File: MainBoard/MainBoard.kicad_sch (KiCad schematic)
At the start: 96 parts, among them J1 KH-TYPE-C-16P, Q1 PMV19XNEAR, Q2 PMV19XNEAR, Q3 PMV19XNEAR, Q4 PMV19XNEAR, U1 INA185A4IDRLR, U10 SI3477DV-T1-GE3, U11 INA185A4IDRLR, U12 SI3477DV-T1-GE3, U2 SI3477DV-T1-GE3, U3 STM32L496VGY6PTR, U4 FUSB302BMPX, U5 BNO086, U6 TPS63802DLAR, U7 SI3477DV-T1-GE3, U8 BQ25756ERRVR, U9 TCAN332DCNR, Y1 9HT11-32.768KBZF-T

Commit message: imu changed from crystal to external mcu clock- yoshita
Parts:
- removed C24, C25: 22pF, Capacitor_SMD:C_0402_1005Metric, symbol Device:C
- removed Y1: 9HT11-32.768KBZF-T, Crystal:Crystal_SMD_2012-2Pin_2.0x1.2mm_HandSoldering, symbol Device:Crystal
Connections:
- net +3.3V: now also U5.10 (CLKSEL0), U5.26 (XOUT32/CLKSEL1)
- net IMU_MCO: now reaches U3.E1 (PC8)
- net IMU_MCO: now also U5.27 (XIN32)
- no-connect marks 23 -> 22

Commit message: Fixed values/issues on BQ chip
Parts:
- R19: value 25k -> 50k
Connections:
- net BAT_SIDE_INDUC: now also C42.1; no longer C42.2, U8.20 (BTST2)
- net EXTERNAL_SIDE_INDUC: no longer U8.26 (BTST1)
- net GND: no longer C41.2, C42.1
- new net: C42.2, U8.20 (BTST2)
- new net: C41.2, U8.26 (BTST1)
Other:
- moved on the sheet: C41, C42
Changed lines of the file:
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@@
 	)
 	(junction
-		(at 480.06 187.96)
-		(diameter 0)
-		(color 0 0 0 0)
-	)
-	(junction
 		(at 234.95 187.96)
 		(diameter 0)
@@
 	)
 	(junction
-		(at 478.79 185.42)
-		(diameter 0)
-		(color 0 0 0 0)
-	)
-	(junction
 		(at 354.33 205.74)
 		(diameter 0)
@@
 	(wire
 		(pts
-			(xy 480.06 187.96) (xy 483.87 187.96)
-		)
-		(stroke
-			(width 0)
-			(type default)
-		)
-	)
-	(wire
-		(pts
 			(xy 383.54 306.07) (xy 414.02 306.07)
 		)
@@
 	(wire
 		(pts
-			(xy 478.79 185.42) (xy 483.87 185.42)
-		)
-		(stroke
-			(width 0)
-			(type default)
-		)
-	)
-	(wire
-		(pts
 			(xy 214.63 203.2) (xy 220.98 203.2)
 		)
@@
 	(wire
 		(pts
+			(xy 476.25 185.42) (xy 483.87 185.42)
+		)
+		(stroke
+			(width 0)
+			(type default)
+		)
+	)
+	(wire
+		(pts
 			(xy 427.99 266.7) (xy 434.34 266.7)
 		)
@@
 	(wire
 		(pts
-			(xy 427.99 187.96) (xy 480.06 187.96)
+			(xy 427.99 187.96) (xy 476.25 187.96)
 		)
 		(stroke
@@
 	(wire
 		(pts
-			(xy 427.99 185.42) (xy 478.79 185.42)
+			(xy 427.99 185.42) (xy 468.63 185.42)
 		)
 		(stroke
@@
 	(wire
 		(pts
+			(xy 483.87 187.96) (xy 500.38 187.96)
+		)
+		(stroke
+			(width 0)
+			(type default)
+		)
+	)
+	(wire
+		(pts
 			(xy 351.79 212.09) (xy 344.17 212.09)
 		)
@@
 	(wire
 		(pts
-			(xy 478.79 182.88) (xy 478.79 185.42)
-		)
-		(stroke
-			(width 0)
-			(type default)
-		)
-	)
-	(wire
-		(pts
 			(xy 220.98 322.58) (xy 223.52 322.58)
 		)
@@
 	(global_label "BAT_SIDE_INDUC"
 		(shape input)
-		(at 483.87 187.96 0)
+		(at 500.38 187.96 0)
 		(fields_autoplaced yes)
 		(effects
@@
 		)
 		(property "Intersheetrefs" "${INTERSHEET_REFS}"
-			(at 502.1557 187.96 0)
+			(at 518.6657 187.96 0)
 			(effects
 				(font
@@
 	)
 	(symbol
-		(lib_id "power:GND")
-		(at 480.06 195.58 0)
-		(unit 1)
-		(exclude_from_sim no)
-		(in_bom yes)
-		(on_board yes)
-		(dnp no)
-		(fields_autoplaced yes)
-		(property "Reference" "#PWR064"
-			(at 480.06 201.93 0)
-			(effects
-				(font
-					(size 1.27 1.27)
-				)
-				(hide yes)
-			)
-		)
-		(property "Value" "GND"
-			(at 480.06 200.66 0)
-			(effects
-				(font
-					(size 1.27 1.27)
-				)
-			)
-		)
-		(property "Footprint" ""
-			(at 480.06 195.58 0)
-			(effects
-				(font
-					(size 1.27 1.27)
-				)
-				(hide yes)
-			)
-		)
-		(property "Datasheet" ""
-			(at 480.06 195.58 0)
-			(effects
-				(font
-					(size 1.27 1.27)
-				)
-				(hide yes)
-			)
-		)
-		(property "Description" "Power symbol creates a global label with name \"GND\" , ground"
-			(at 480.06 195.58 0)
-			(effects
-				(font
-					(size 1.27 1.27)
-				)
-				(hide yes)
-			)
-		)
-		(pin "1"
-		)
-		(instances
-			(project "MainBoard"
-				(path "/6b5bd430-8554-421d-a2d3-13f7e8cab430"
-					(reference "#PWR064")
-					(unit 1)
-				)
-			)
-		)
-	)
-	(symbol
 		(lib_id "Device:C")
 		(at 171.45 383.54 0)
@@
 			)
 		)
-		(property "Value" "25k"
+		(property "Value" "50k"
 			(at 362.204 213.868 90)
 			(effects
@@
 	(symbol
 		(lib_id "Device:C")
-		(at 478.79 179.07 180)
+		(at 472.44 185.42 270)
 		(unit 1)
 		(exclude_from_sim no)
@@
 		(dnp no)
 		(property "Reference" "C41"
-			(at 484.632 180.086 0)
+			(at 472.186 179.832 90)
 			(effects
 				(font
@@
 		)
 		(property "Value" "100nF"
-			(at 484.632 177.546 0)
+			(at 472.948 181.864 90)
 			(effects
 				(font
@@
 		)
 		(property "Footprint" "Capacitor_SMD:C_0402_1005Metric"
-			(at 477.8248 175.26 0)
+			(at 468.63 186.3852 0)
 			(effects
 				(font
@@
 		)
 		(property "Datasheet" "~"
-			(at 478.79 179.07 0)
+			(at 472.44 185.42 0)
 			(effects
 				(font
@@
 		)
 		(property "Description" "Unpolarized capacitor"
-			(at 478.79 179.07 0)
+			(at 472.44 185.42 0)
 			(effects
 				(font
@@
 	)
 	(symbol
-		(lib_id "power:GND")
-		(at 478.79 175.26 180)
-		(unit 1)
-		(exclude_from_sim no)
-		(in_bom yes)
-		(on_board yes)
-		(dnp no)
-		(fields_autoplaced yes)
-		(property "Reference" "#PWR063"
-			(at 478.79 168.91 0)
-			(effects
-				(font
-					(size 1.27 1.27)
-				)
-				(hide yes)
-			)
-		)
-		(property "Value" "GND"
-			(at 478.79 170.18 0)
-			(effects
-				(font
-					(size 1.27 1.27)
-				)
-			)
-		)
-		(property "Footprint" ""
-			(at 478.79 175.26 0)
-			(effects
-				(font
-					(size 1.27 1.27)
-				)
-				(hide yes)
-			)
-		)
-		(property "Datasheet" ""
-			(at 478.79 175.26 0)
-			(effects
-				(font
-					(size 1.27 1.27)
-				)
-				(hide yes)
-			)
-		)
-		(property "Description" "Power symbol creates a global label with name \"GND\" , ground"
-			(at 478.79 175.26 0)
-			(effects
-				(font
-					(size 1.27 1.27)
-				)
-				(hide yes)
-			)
-		)
-		(pin "1"
-		)
-		(instances
-			(project "MainBoard"
-				(path "/6b5bd430-8554-421d-a2d3-13f7e8cab430"
-					(reference "#PWR063")
-					(unit 1)
-				)
-			)
-		)
-	)
-	(symbol
 		(lib_id "inspirefly:INA185A1IDRLR")
 		(at 346.71 114.3 0)
@@
 	(symbol
 		(lib_id "Device:C")
-		(at 480.06 191.77 180)
+		(at 480.06 187.96 270)
 		(unit 1)
 		(exclude_from_sim no)
@@
 		(dnp no)
 		(property "Reference" "C42"
-			(at 485.648 193.04 0)
+			(at 484.378 189.484 90)
 			(effects
 				(font
@@
 		)
 		(property "Value" "100nF"
-			(at 485.648 190.5 0)
+			(at 484.378 192.024 90)
 			(effects
 				(font
@@
 		)
 		(property "Footprint" "Capacitor_SMD:C_0402_1005Metric"
-			(at 479.0948 187.96 0)
+			(at 476.25 188.9252 0)
 			(effects
 				(font
@@
 		)
 		(property "Datasheet" "~"
-			(at 480.06 191.77 0)
+			(at 480.06 187.96 0)
 			(effects
 				(font
@@
 		)
 		(property "Description" "Unpolarized capacitor"
-			(at 480.06 191.77 0)
+			(at 480.06 187.96 0)
 			(effects
 				(font

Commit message: Footprint edits and board setup
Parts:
- added TP1: BatBeforeCutoff, TestPoint:TestPoint_Pad_D1.0mm, symbol Connector:TestPoint
- added TP2: Bat+, TestPoint:TestPoint_Pad_D1.0mm, symbol Connector:TestPoint
- added TP3: 3.3V, TestPoint:TestPoint_Pad_D1.0mm, symbol Connector:TestPoint
- added TP4, TP5, TP6: GND, TestPoint:TestPoint_Pad_D1.0mm, symbol Connector:TestPoint
- JP1: footprint Jumper:SolderJumper-2_P1.3mm_Open_TrianglePad1.0x1.5mm -> inspirefly:SmallJumper
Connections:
- net +3.3V: now also TP3.1
- net BAT+: now also TP2.1
- net GND: now also TP4.1, TP5.1, TP6.1
- net at BT1.P, BT2.P, R13.2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: now also TP1.1

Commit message: Added a good amount of STM connections
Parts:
- removed R22: 250k, Resistor_SMD:R_0402_1005Metric, symbol Device:R_US
- added C24, C25: 100nF, Capacitor_SMD:C_0402_1005Metric, symbol Device:C_Small
- added R1, R2: 1k, Resistor_SMD:R_0402_1005Metric, symbol Device:R_US
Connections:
- net H_MDSI_MCUMOSI is gone; now on net H_MDSI_SPI1_MOSI: U5.17 (SA0/H_MOSI)
- net IMU_CSN_GPIO is gone; now on net IMU_SP1_NSS: U5.18 (H_CSN)
- net IMU_MCU_MISO is gone; now on net IMU_MCU_SPI1_MISO: U5.20 (H_SDA/H_MISO/TX)
- net IMU_MCU_SLK is gone; now on net IMU_MCU_SPI1_SCK: U5.19 (H_SCL/SCK/RX)
- net +3.3V: no longer U5.26 (XOUT32/CLKSEL1)
- net ADC1_A1: now also R1.1
- net ADC1_A2: now also R2.1
- net CAN_RXD: now also U3.B3 (PD0)
- net CAN_TXD: now also U3.A3 (PD1)
- net GND: now also U5.26 (XOUT32/CLKSEL1), U8.10 (ILIM_HIZ), C24.1, C25.2
- net I2C1_SCL: now also U3.B8 (PB8)
- net I2C1_SDA: now also U3.A8 (PB9)
- net I2C2_SCL: now also U3.H2 (PB13)
- net I2C2_SDA: now also U3.H1 (PB14)
- net I2C3_SCL: now also U3.G10 (PC0)
- net I2C3_SDA: now also U3.F7 (PC1)
- net I2C4_SCL: now also U3.A7 (PB6)
- net I2C4_SDA: now also U3.B7 (PB7)
- net IMU_PS0/WAKE_GPIO: no longer U3.G8 (PA0)
- net USB_D+: now also U3.C1 (PA12)
- net USB_D-: now also U3.D1 (PA11)
- net PARENT_SPI3_MISO: now reaches U3.A5 (PG10)
- net PARENT_SPI3_NSS: now reaches U3.B6 (PG12)
- net PARENT_SPI3_SCK: now reaches U3.D6 (PG9)
- net PARENT_SPI3_MOSI: now reaches U3.E5 (PG11)
- net ANT_SPI2_MOSI: now reaches U3.F6 (PC3)
- net H_MDSI_SPI1_MOSI: now reaches U3.G6 (PA7)
- net at U3.G7 (PA1): now also C24.2, R1.2
- net ANT_SPI2_MISO: now reaches U3.G9 (PC2)
- net IMU_SP1_NSS: now reaches U3.H7 (PA4)
- net at U3.H8 (PA2): now also C25.1, R2.2
- net ANT_SPI2_NSS: now reaches U3.J1 (PB12)
- net IMU_MCU_SPI1_SCK: now reaches U3.J7 (PA5)
- net ANT_SPI2_SCK: now reaches U3.K3 (PB10)
- net IMU_MCU_SPI1_MISO: now reaches U3.K9 (PA6)
- net IMU_NRST: now reaches U5.11 (NRST)
- net BQ_INT_DIN renamed BATMANG_INT_DIN
- net IMU_MCO: no longer names the net of U3.E1 (PC8)
- net IMU_MCO: no longer U5.27 (XIN32)
- net INT_N renamed USBC_PD_INT_N
- no-connect marks 22 -> 23
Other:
- moved on the sheet: U3A

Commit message: Pushing more schematic changes
Added ST link connections
Added Harwin M55
Changed some items for Battery managment
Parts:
- removed J1: KH-TYPE-C-16P, inspirefly:KINGHELM_KH-TYPE-C-16P, symbol inspirefly:KH-TYPE-C-16P
- added C29, C46: 22pF, Capacitor_SMD:C_0402_1005Metric, symbol Device:C_Small
- added J1: 0015912060 Molex, inspirefly:CONN_713080000-SD_06_M6p10_MOL, symbol Connector:Conn_01x06_Pin
- added J2: USB4110-GF-A, USB4110-GF-A_GCT, symbol inspirefly:USB4110-GF-A
- added J3: M55-7104042R, inspirefly:HARWIN_M55-7104042R, symbol inspirefly:M55-7104042R
- added R22: 100k, Resistor_SMD:R_0402_1005Metric, symbol Device:R_US
- added SW1, SW2: SW_TL1015AF160QG, inspirefly:SW_TL1015AF160QG, symbol Switch:SW_Push
- added Y1: XTAL_ABS07-32.768KHZ-T, inspirefly:XTAL_ABS07-32.768KHZ-T, symbol Device:Crystal
- L2: value 4.7uH -> 2.2uH; footprint inspirefly:WE-LQSA_5040 -> inspirefly:IHLP1212BZEZ2R2M1Z
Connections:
- net +3.3V: now also J1.5 (Pin_5), SW2.2
- net ANT_SPI2_MISO: now also J3.A15
- net ANT_SPI2_MOSI: now also J3.A16
- net ANT_SPI2_NSS: now also J3.A14
- net ANT_SPI2_SCK: now also J3.A13
- net BOARD_OUT_3.3V: now also J3.B1, J3.B2, J3.B3
- net BOARD_OUT_BAT: now also J3.B6, J3.B7, J3.B8
- net CAN_H: now also J3.A18
- net CAN_L: now also J3.A20
- net EXTERNAL_VOLTAGE: now also J3.B11, J3.B12, J3.B13, J3.B14
- net GND: now also C29.1, C46.1, J1.6 (Pin_6), J2.15 (Shield), J2.16 (Shield), J2.17 (Shield), J2.18 (Shield), J2.A1-B12 (GND), J2.A12-B1 (GND), J3.A17, J3.A19, J3.B10, J3.B18, J3.B20, J3.B4, J3.B5, J3.B9, J3.SH1 (Shield), J3.SH2 (Shield), J3.SH3 (Shield), J3.SH4 (Shield), R22.1, SW1.2
- net I2C1_SCL: now also J3.A7
- net I2C1_SDA: now also J3.A8
- net I2C2_SCL: now also J3.A5
- net I2C2_SDA: now also J3.A6
- net I2C3_SCL: now also J3.A3
- net I2C3_SDA: now also J3.A4
- net I2C4_SCL: now also J3.A1
- net I2C4_SDA: now also J3.A2
- net PARENT_SPI3_MISO: now also J3.A10
- net PARENT_SPI3_MOSI: now also J3.A11
- net PARENT_SPI3_NSS: now also J3.A12
- net PARENT_SPI3_SCK: now also J3.A9
- net USB_D+: now also J2.A6 (DP1), J2.B6 (DP2)
- net USB_D-: now also J2.A7 (DN1), J2.B7 (DN2)
- net at D1.2 (A), U4.2 (VBUS): now also J2.A4-B9 (VBUS), J2.A9-B4 (VBUS)
- net at C7.1, U4.11 (CC1): now also J2.A5 (CC1)
- net at C6.1, U4.14 (CC2): now also J2.B5 (CC2)
- net JTCK/SWCLK: now reaches U3.B2 (PA14)
- net JTCK/SWCLK: now also J1.2 (Pin_2)
- net JTMS/SWDIO: now reaches U3.C2 (PA13)
- net JTMS/SWDIO: now also J1.1 (Pin_1)
- net at U3.D10 (PC14-OSC32_IN): now also C46.2, Y1.2
- net BOOT0: now reaches U3.D7 (PH3-BOOT0)
- net BOOT0: now also R22.2, SW2.1
- net at U3.D9 (PC15-OSC32_OUT): now also C29.2, Y1.1
- net SWO: now reaches U3.F5 (PB3)
- net SWO: now also J1.3 (Pin_3)
- net NRST: now reaches U3.F8 (NRST)
- net NRST: now also J1.4 (Pin_4), SW1.1
- no-connect marks 23 -> 25
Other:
- note added: "Debug + ST-Link"
- note added: "IHLP1212BZEZ2R2M1Z"
- note removed: "Wurth 78404054047"
- moved on the sheet: C24, R1, U2

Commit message: Did some placement
Did most the caps for MCU, general placement for fill zones
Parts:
- C34, C35: footprint Capacitor_SMD:C_0402_1005Metric -> Capacitor_SMD:C_1206_3216Metric_Pad1.33x1.80mm_HandSolder
- J2: footprint USB4110-GF-A_GCT -> inspirefly:USB4110-GF-A_GCT
- R21: footprint Resistor_SMD:R_0402_1005Metric -> Resistor_SMD:R_1206_3216Metric_Pad1.30x1.75mm_HandSolder
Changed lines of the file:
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@@
 			)
 		)
-		(property "Footprint" "Resistor_SMD:R_0402_1005Metric"
+		(property "Footprint" "Resistor_SMD:R_1206_3216Metric_Pad1.30x1.75mm_HandSolder"
 			(at 359.664 305.054 90)
 			(effects
@@
 			)
 		)
-		(property "Footprint" "Capacitor_SMD:C_0402_1005Metric"
+		(property "Footprint" "Capacitor_SMD:C_1206_3216Metric_Pad1.33x1.80mm_HandSolder"
 			(at 460.0448 298.45 0)
 			(effects
@@
 			)
 		)
-		(property "Footprint" "USB4110-GF-A_GCT"
+		(property "Footprint" "inspirefly:USB4110-GF-A_GCT"
 			(at 24.13 374.65 0)
 			(effects
@@
 			)
 		)
-		(property "Footprint" "Capacitor_SMD:C_0402_1005Metric"
+		(property "Footprint" "Capacitor_SMD:C_1206_3216Metric_Pad1.33x1.80mm_HandSolder"
 			(at 382.5748 298.45 0)
 			(effects

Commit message: Still waiting on final board size....
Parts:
- added R35: 100k, Resistor_SMD:R_0402_1005Metric, symbol Device:R_US
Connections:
- net BAT+: now also U2.4 (S), R35.2
- net BATMANG_INT_DIN: now also U3.J5 (PE9)
- net BAT_PULLDOWN: now also U3.F3 (PD14)
- net EXTERNAL_3.3V_CUTOFF: now also U3.K4 (PE11)
- net EXTERNAL_BAT_CUTOFF: now also U3.E4 (PC7)
- net IMU_NRST: now also U3.G4 (PE14)
- net IMU_PSO/WAKE_GPIO: now also U3.H4 (PE15), U3.K5 (PE8)
- net USBC_PD_INT_N: now also U3.K6 (PE7)
- net HEATER_ENABLE: now reaches U3.E1 (PC8)
- net HEATER_ENABLE: now also U2.3 (G), R35.1
- no-connect marks 25 -> 65

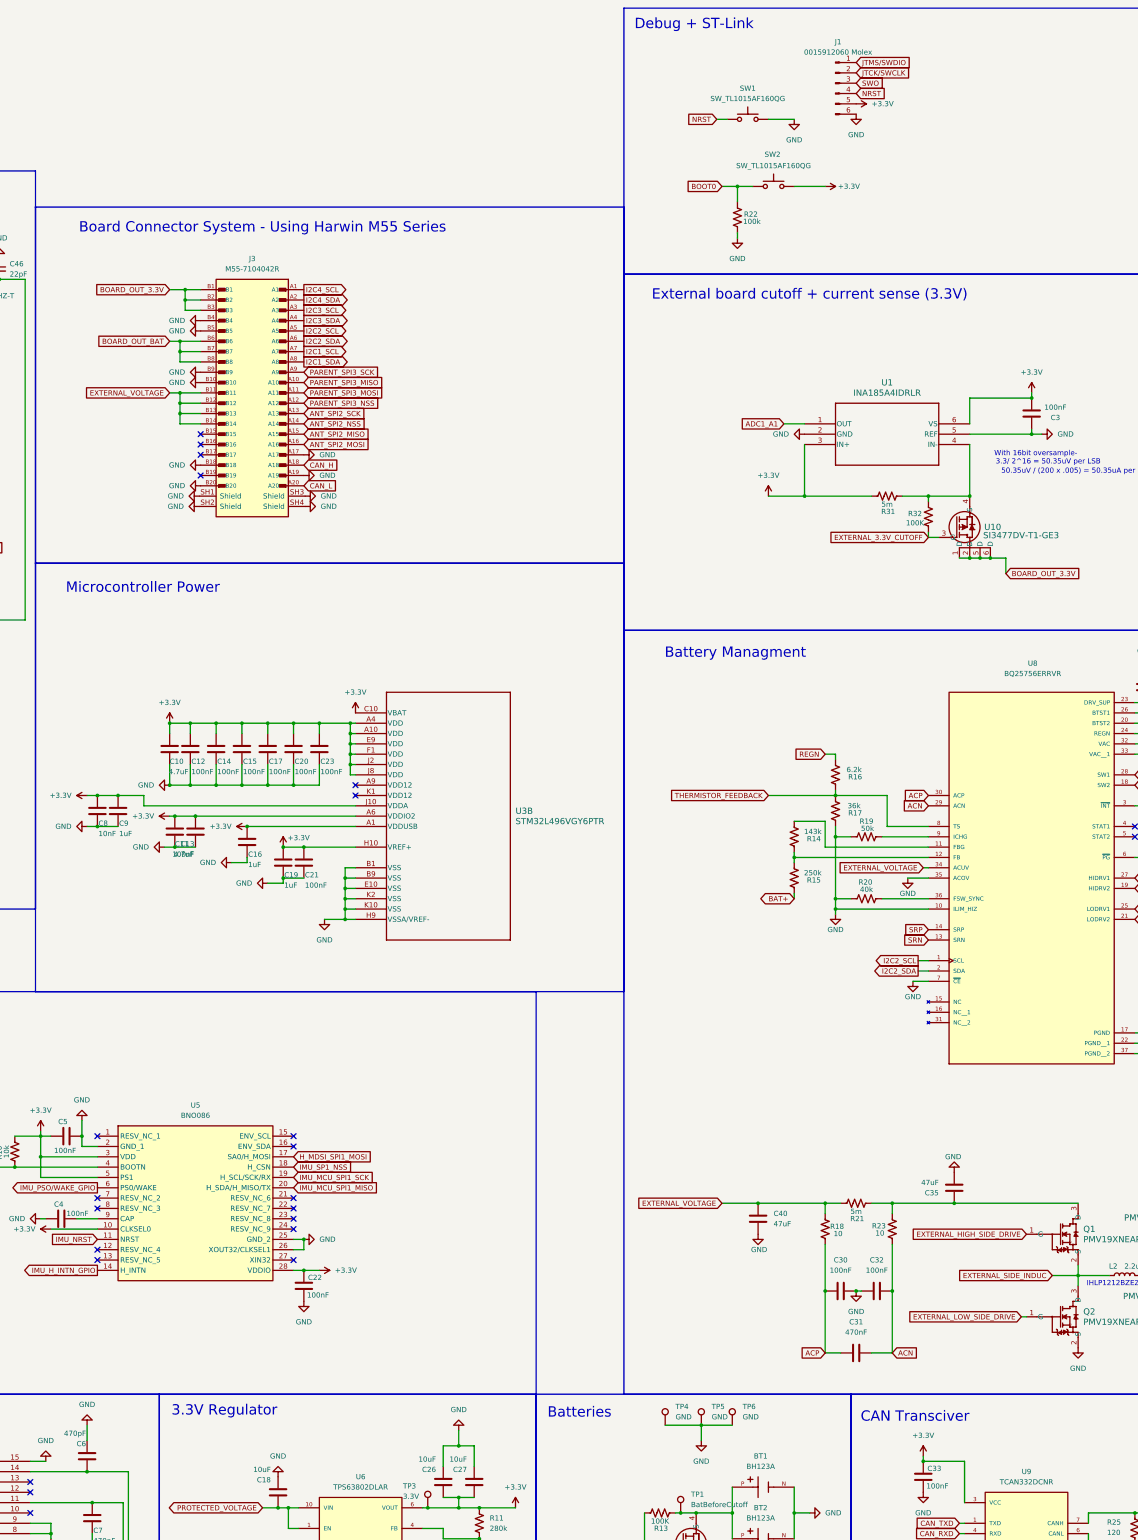
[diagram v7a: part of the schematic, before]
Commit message: Happy with placement
Got sizes from mechanical, adjusted placement accordingly
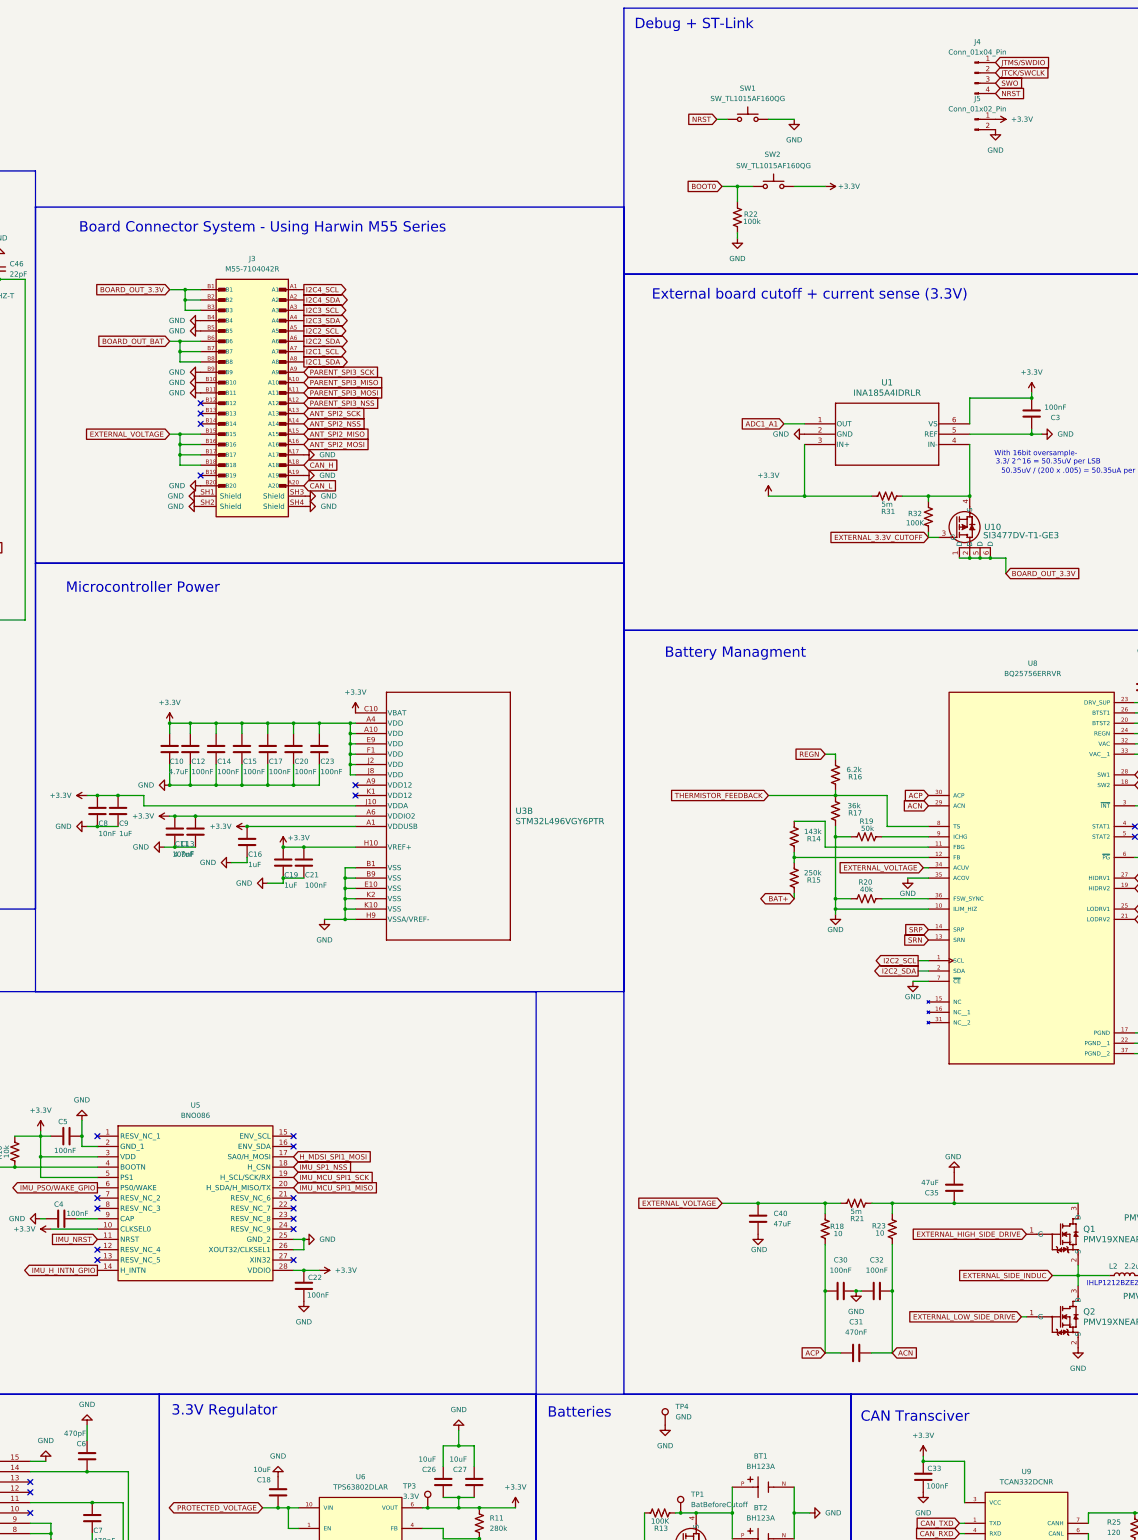
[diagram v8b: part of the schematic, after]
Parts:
- removed J1: 0015912060 Molex, inspirefly:CONN_713080000-SD_06_M6p10_MOL, symbol Connector:Conn_01x06_Pin
- removed TP5, TP6: GND, TestPoint:TestPoint_Pad_D1.0mm, symbol Connector:TestPoint
- added J4: Conn_01x04_Pin, Connector_PinHeader_2.54mm:PinHeader_2x02_P2.54mm_Vertical, symbol Connector:Conn_01x04_Pin
- added J5: Conn_01x02_Pin, Connector_PinHeader_2.54mm:PinHeader_1x02_P2.54mm_Vertical, symbol Connector:Conn_01x02_Pin
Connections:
- net +3.3V: now also J5.1 (Pin_1)
- net EXTERNAL_VOLTAGE: now also J3.B15, J3.B16, J3.B17, J3.B18; no longer J3.B11, J3.B12, J3.B13, J3.B14
- net GND: now also J3.B11, J5.2 (Pin_2); no longer J3.B18
- net JTCK/SWCLK: now also J4.2 (Pin_2)
- net JTMS/SWDIO: now also J4.1 (Pin_1)
- net NRST: now also J4.4 (Pin_4)
- net SWO: now also J4.3 (Pin_3)
